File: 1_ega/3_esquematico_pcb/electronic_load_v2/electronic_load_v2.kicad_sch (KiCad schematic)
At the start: 63 parts, among them J1 Encoder, J11 LOAD, J12 Memoria SD, J13 LCD, J15 VCC, J16 RTC, J17 EGB_I2C, J3 GND, J6 RPico PWR, J7 GND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

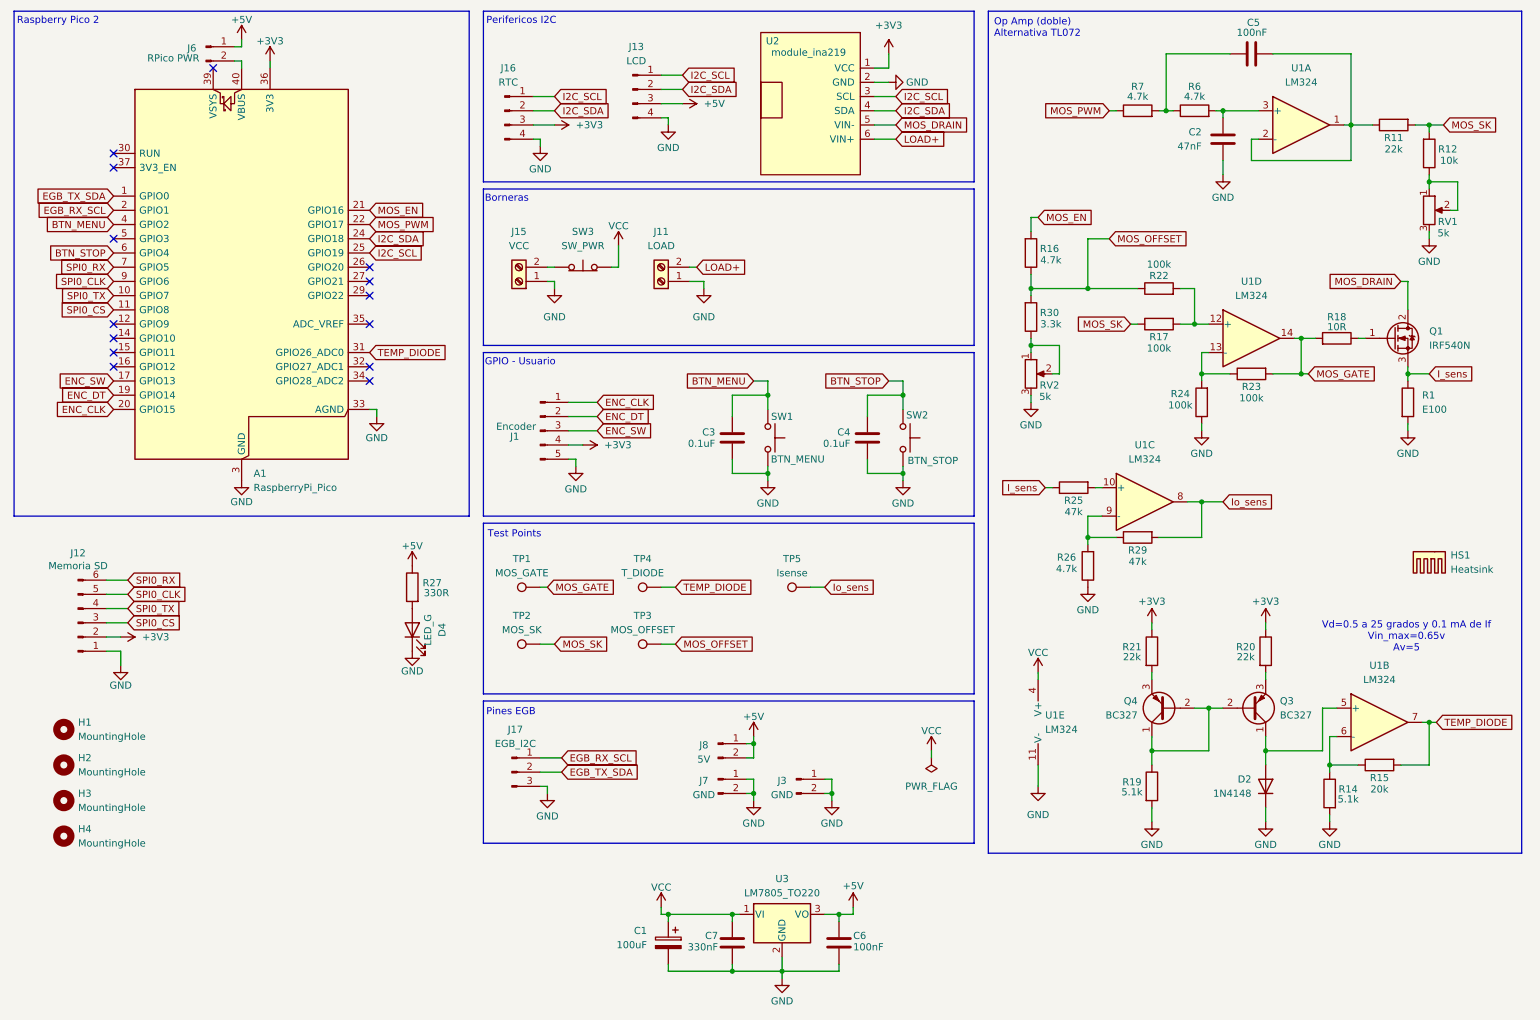
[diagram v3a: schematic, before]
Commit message: chore: ajustar valores de resistencias
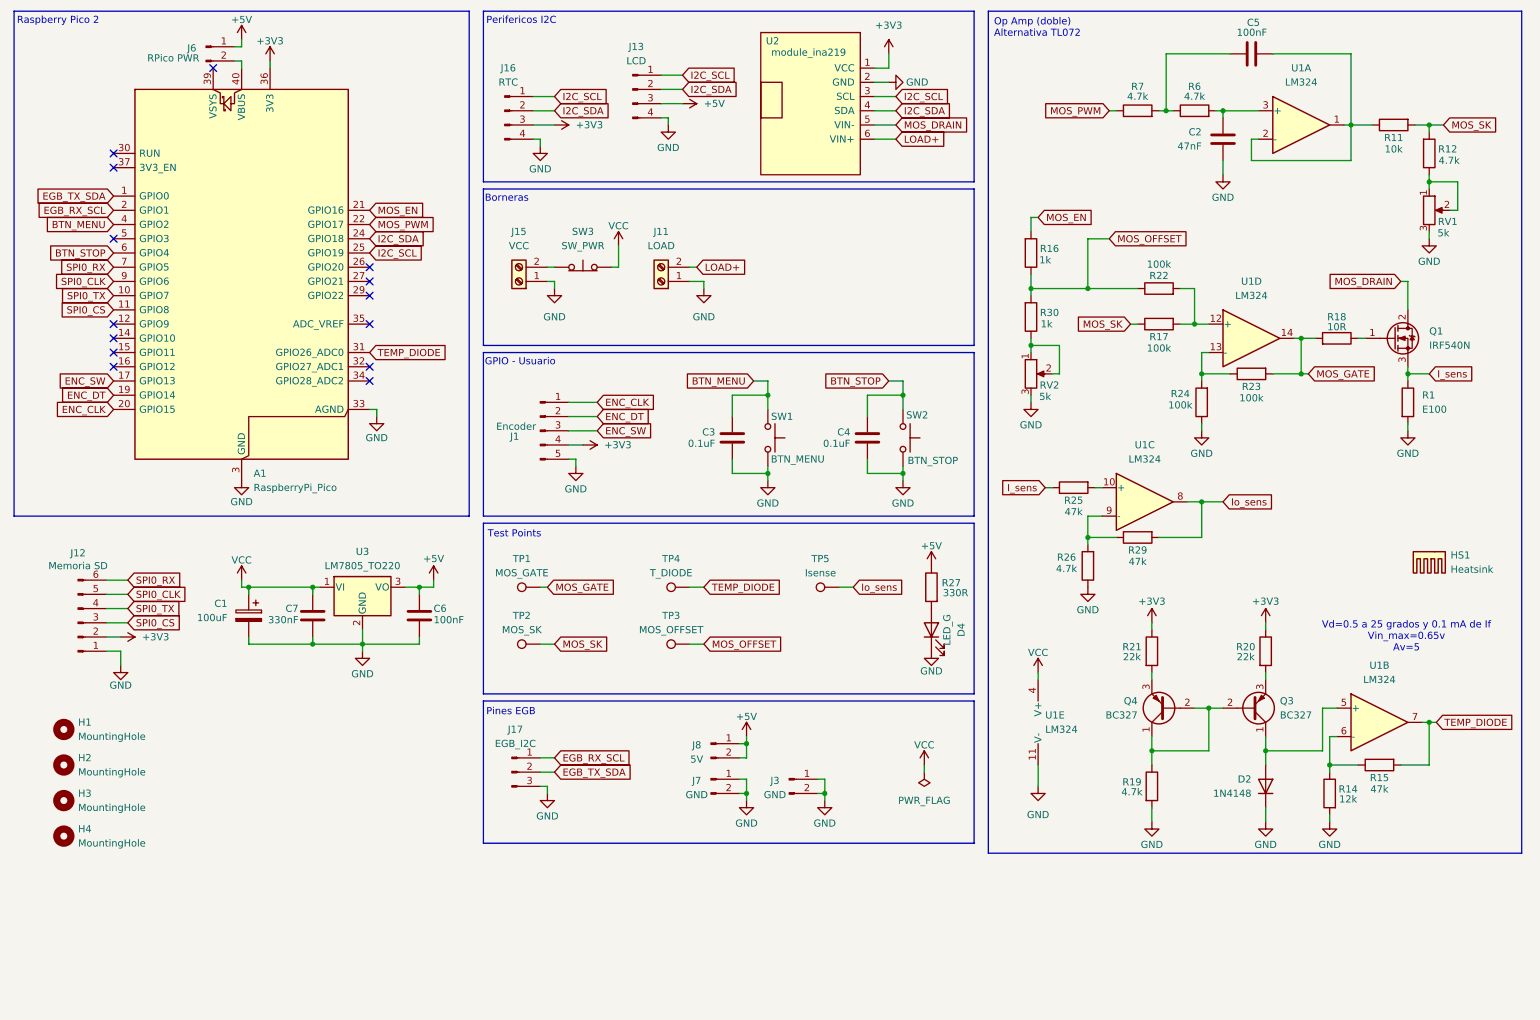
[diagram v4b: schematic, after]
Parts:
- R11: value 22k -> 10k
- R12: value 10k -> 4.7k
- R14: value 5.1k -> 12k
- R15: value 20k -> 47k
- R16: value 4.7k -> 1k
- R19: value 5.1k -> 4.7k
- R30: value 3.3k -> 1k
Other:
- moved on the sheet: C1, C6, C7, D4, J3, J7, J8, R27, TP3, TP4, TP5, U3

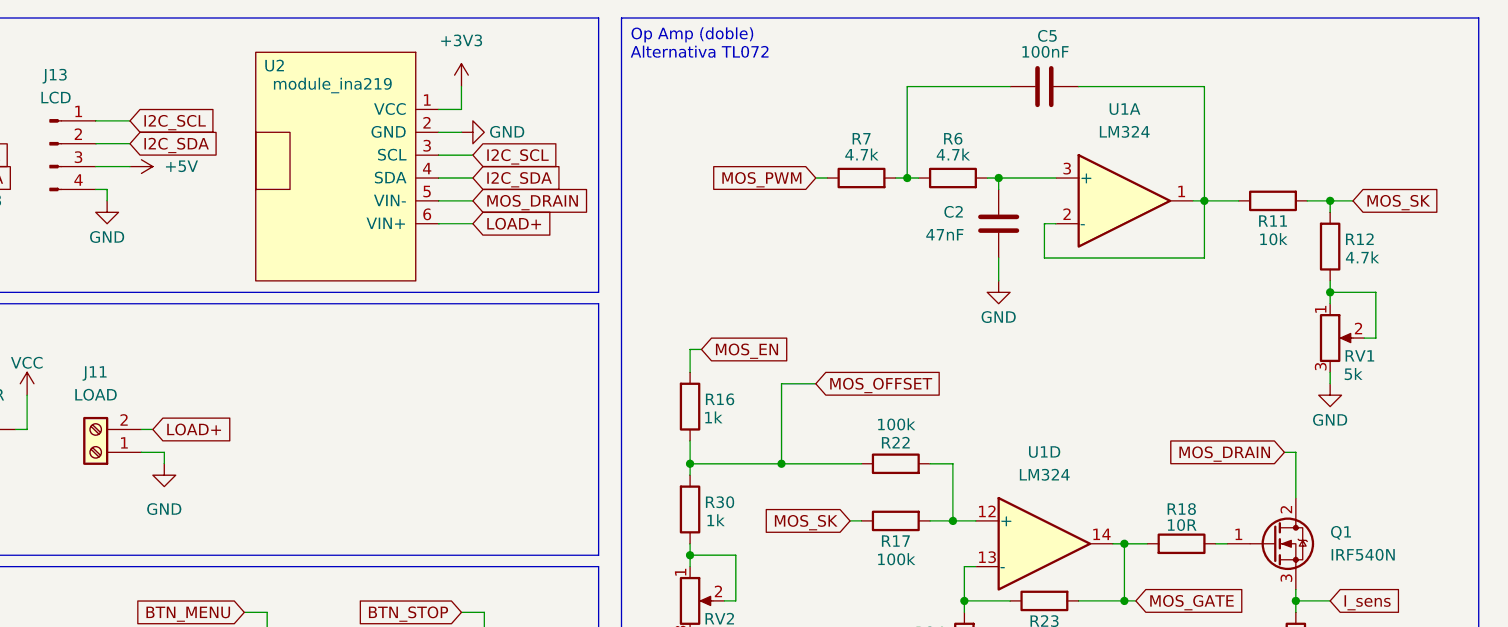
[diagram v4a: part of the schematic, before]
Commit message: perf: ajustes en pistas y clearance para cnc
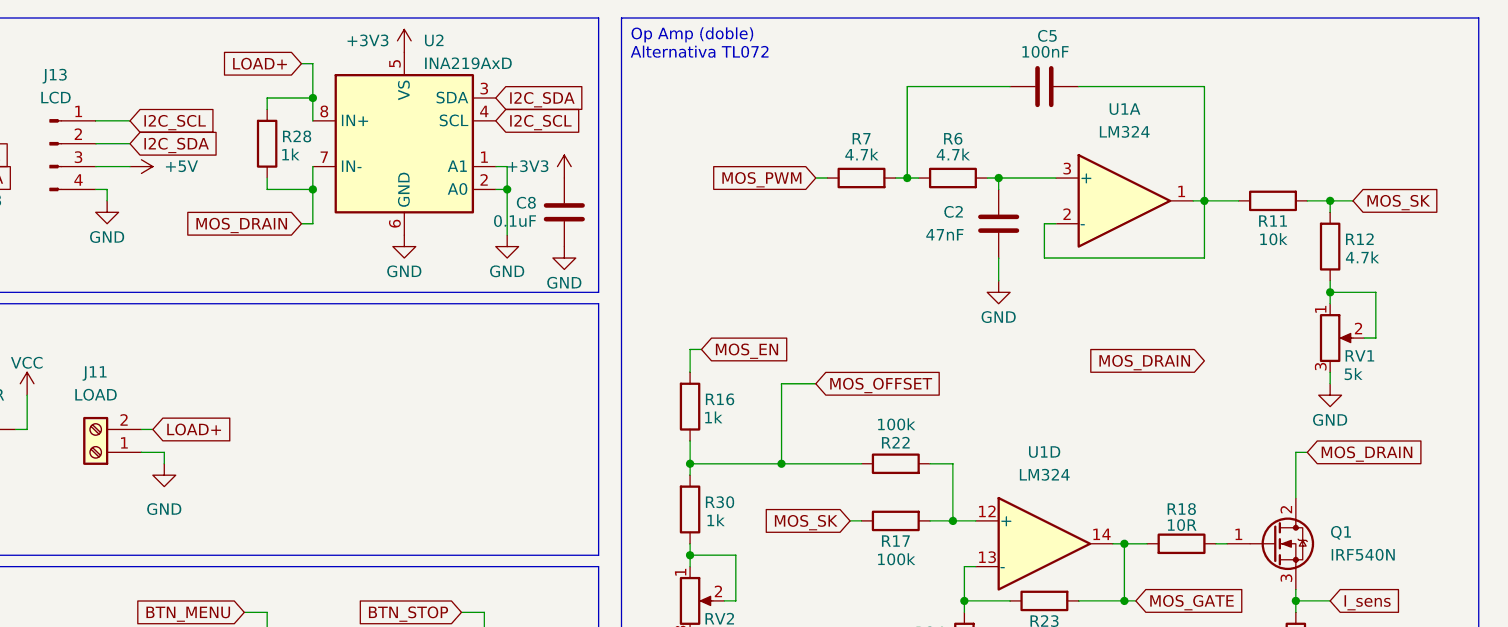
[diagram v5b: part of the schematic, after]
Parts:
- removed U2: module_ina219, usini_sensors:module_ina219, symbol usini_sensors:module_ina219
- added C8: 0.1uF, Capacitor_SMD:C_0805_2012Metric_Pad1.18x1.45mm_HandSolder, symbol Device:C
- added R28: 1k, Resistor_SMD:R_1206_3216Metric_Pad1.30x1.75mm_HandSolder, symbol Device:R
- added U2: INA219AxD, Package_SO:SOIC-8_3.9x4.9mm_P1.27mm, symbol Sensor_Energy:INA219AxD
- R27: footprint Resistor_SMD:R_1206_3216Metric_Pad1.30x1.75mm_HandSolder -> Resistor_SMD:R_0805_2012Metric_Pad1.20x1.40mm_HandSolder
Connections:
- net +3V3: now also C8.2, U2.5 (VS)
- net GND: now also C8.1, U2.1 (A1), U2.2 (A0), U2.6 (GND)
- net I2C_SCL: now also U2.4 (SCL)
- net I2C_SDA: now also U2.3 (SDA)
- net LOAD+: now also R28.2, U2.8 (IN+)
- net MOS_DRAIN: now also R28.1, U2.7 (IN-)

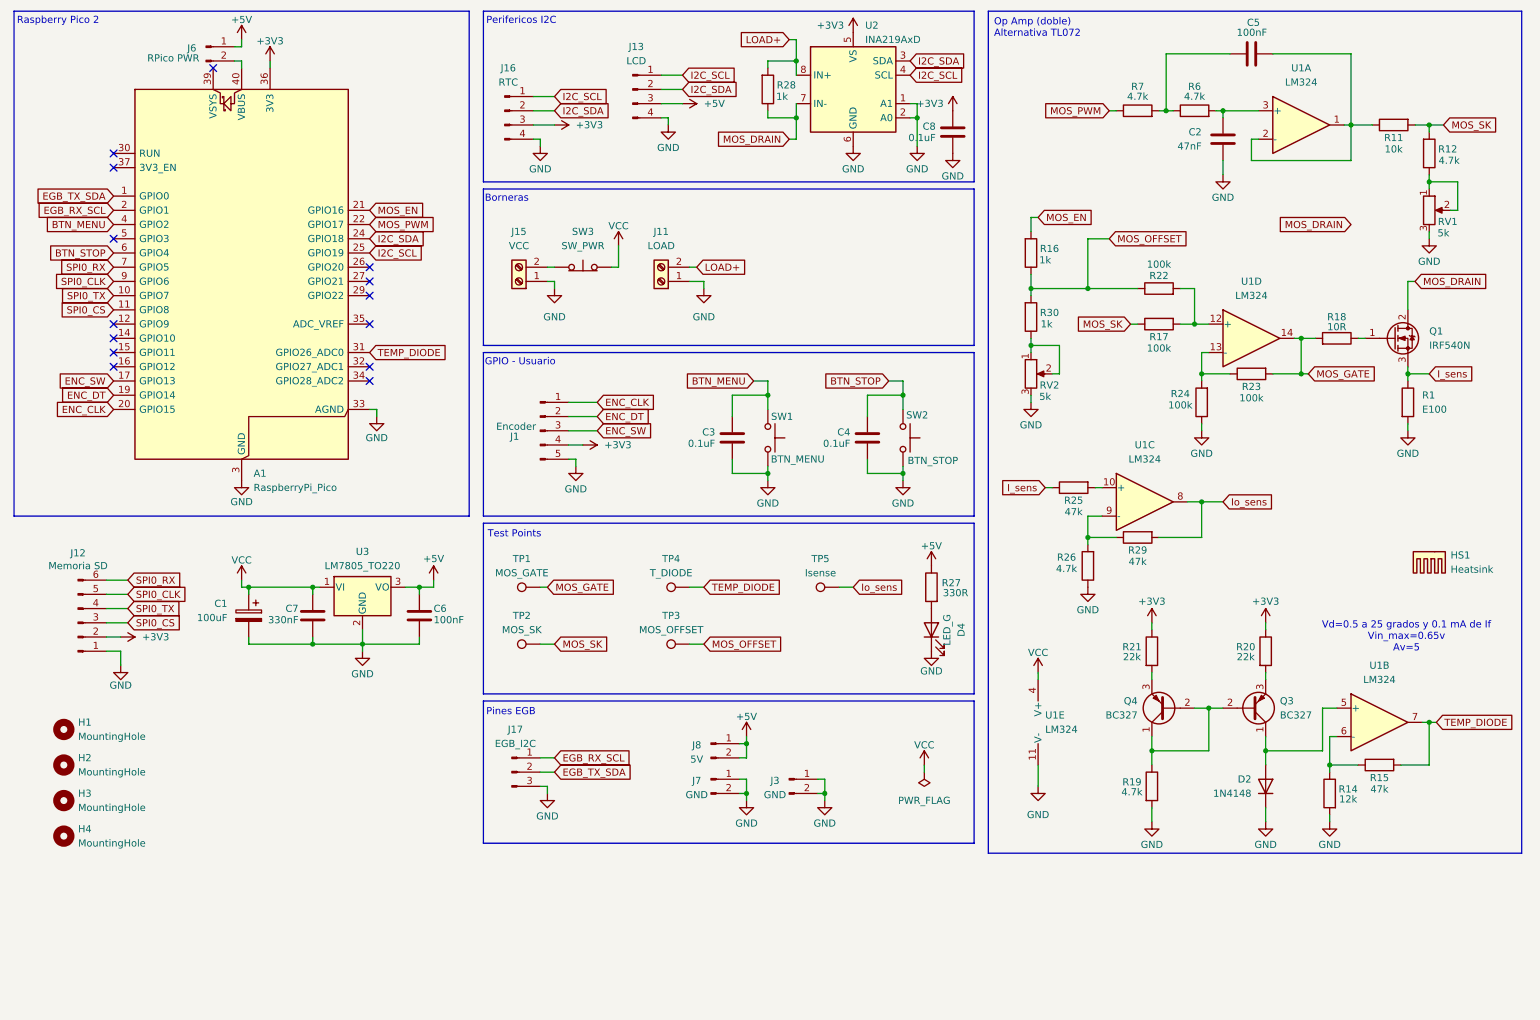
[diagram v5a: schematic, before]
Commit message: fix: footprint de R shunt. chore: separar los componentes en la zona del operacional
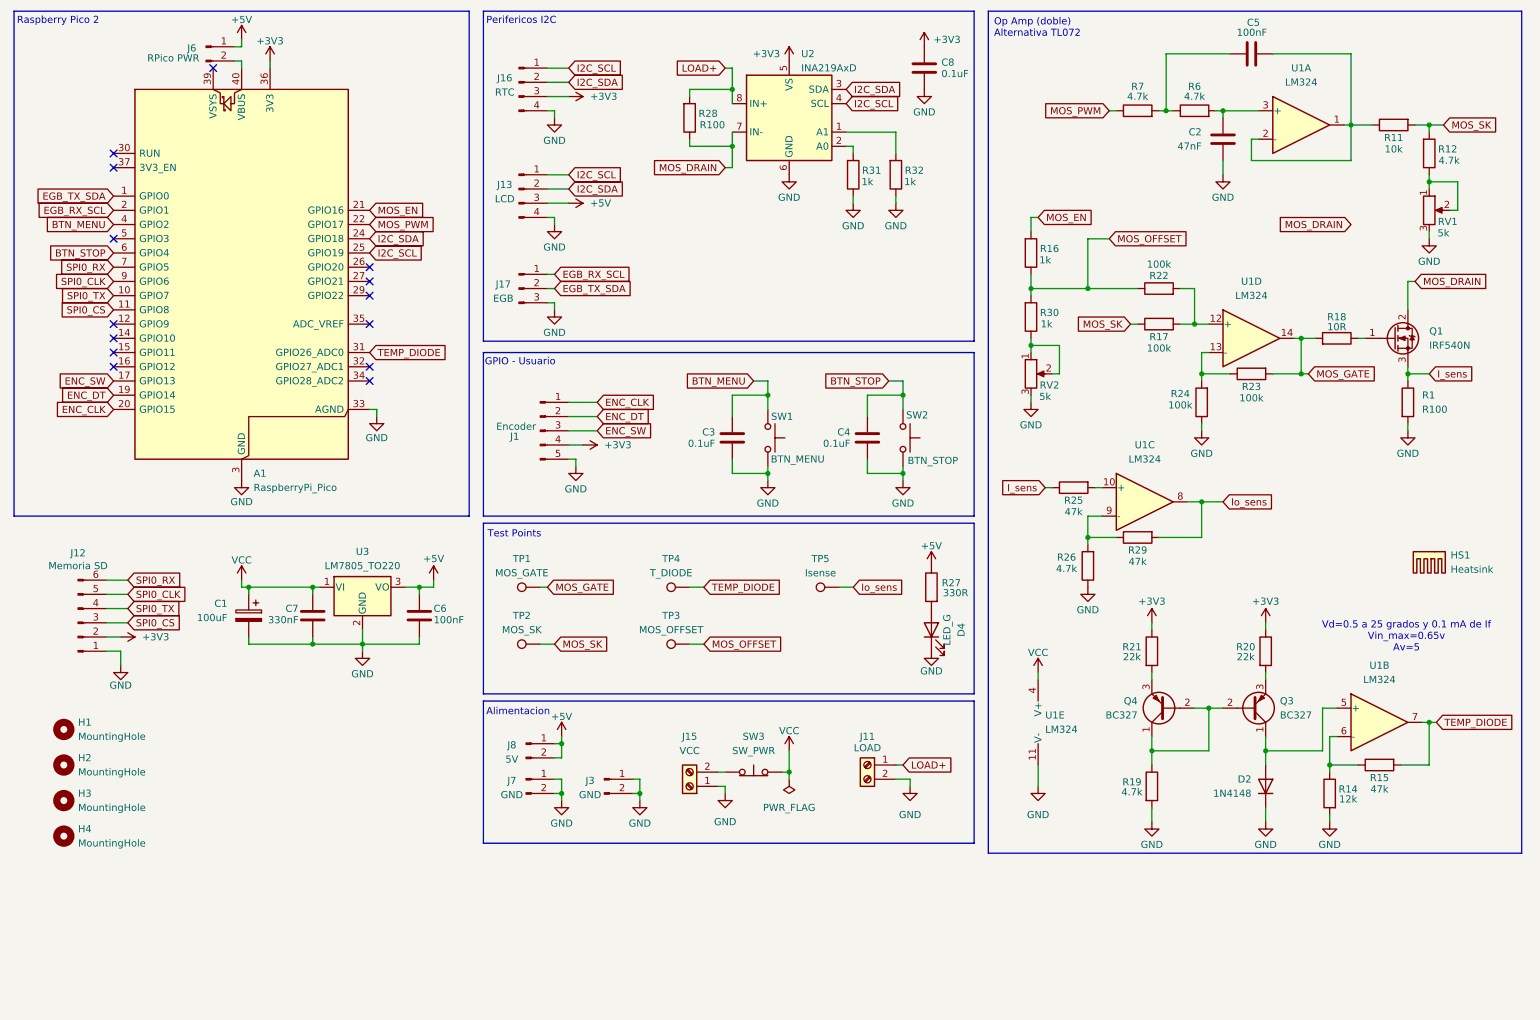
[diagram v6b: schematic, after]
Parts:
- added R31, R32: 1k, Resistor_SMD:R_0805_2012Metric_Pad1.20x1.40mm_HandSolder, symbol Device:R
- J17: value EGB_I2C -> EGB
- R1: value E100 -> R100; footprint Resistor_THT:R_Axial_DIN0309_L9.0mm_D3.2mm_P12.70mm_Horizontal -> Resistor_THT:R_Axial_DIN0922_L20.0mm_D9.0mm_P25.40mm_Horizontal
- R20, R21: footprint Resistor_THT:R_Axial_DIN0207_L6.3mm_D2.5mm_P10.16mm_Horizontal -> Resistor_THT:R_Axial_DIN0207_L6.3mm_D2.5mm_P7.62mm_Horizontal
- R28: value 1k -> R100; footprint Resistor_SMD:R_1206_3216Metric_Pad1.30x1.75mm_HandSolder -> electronic_load:R_shunt_ina219
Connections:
- net GND: now also J11.2 (Pin_2), R31.1, R32.1; no longer J11.1 (Pin_1), U2.1 (A1), U2.2 (A0)
- net LOAD+: now also J11.1 (Pin_1); no longer J11.2 (Pin_2)
- new net: R32.2, U2.1 (A1)
- new net: R31.2, U2.2 (A0)
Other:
- note added: "Alimentacion"
- note removed: "Borneras"
- note removed: "Pines EGB"
- moved on the sheet: C8, J11, J13, J15, J16, J17, J3, J7, J8, R28, SW3, U2
